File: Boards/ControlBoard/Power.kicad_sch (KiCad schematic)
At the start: 36 parts

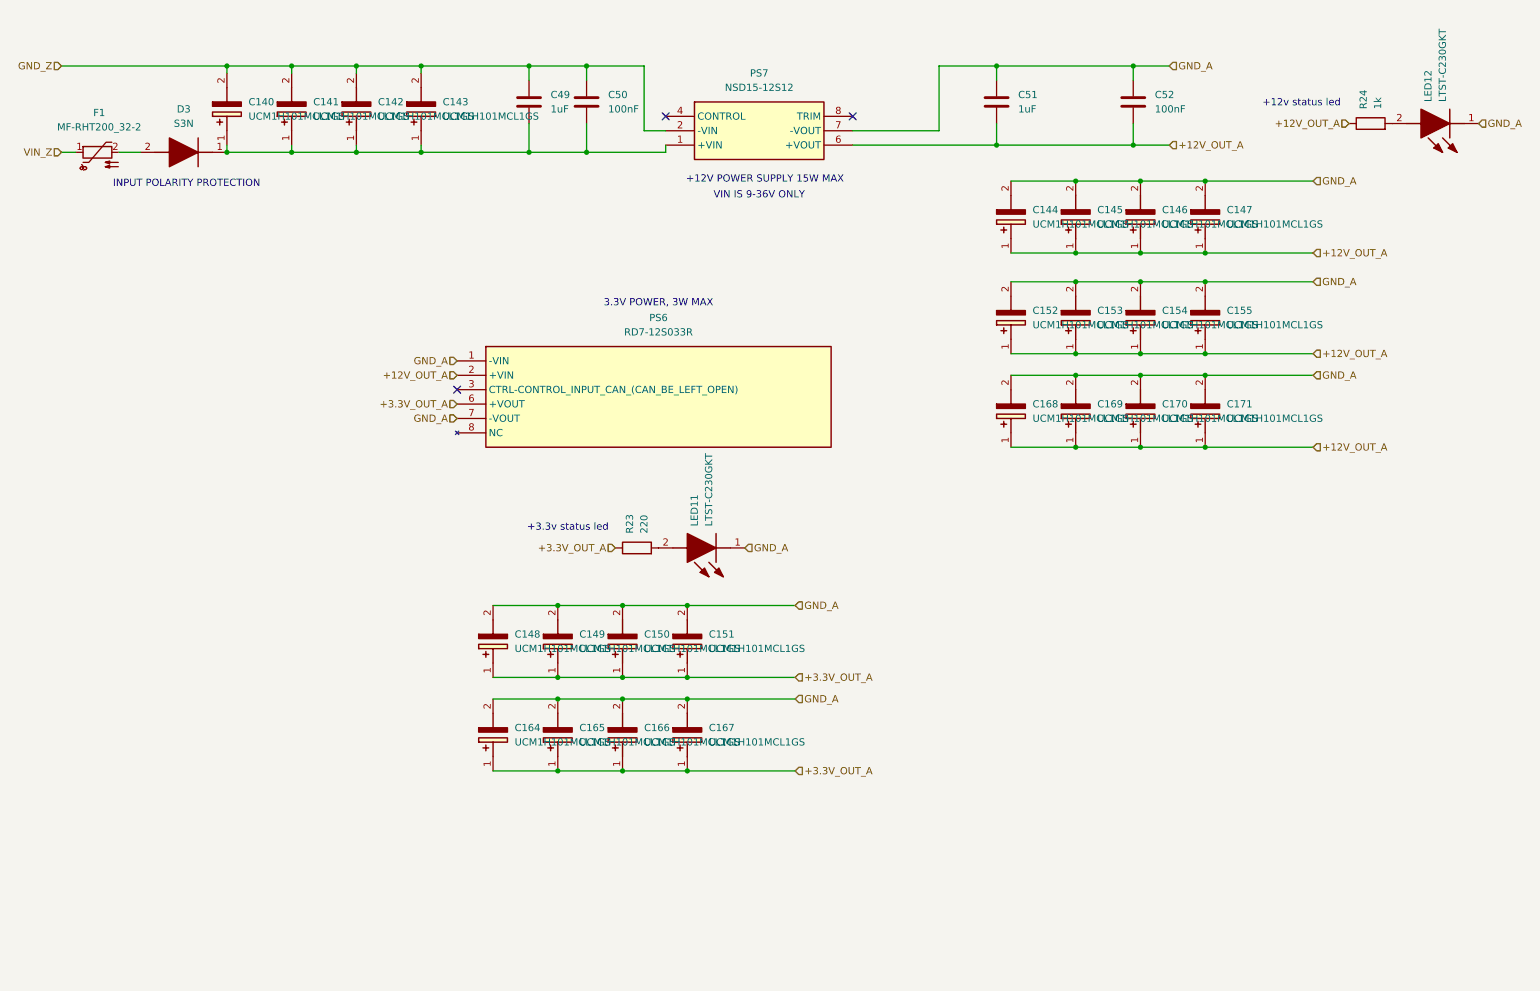
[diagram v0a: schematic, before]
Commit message: layout control boards, add baseplate, refine mechanical layout
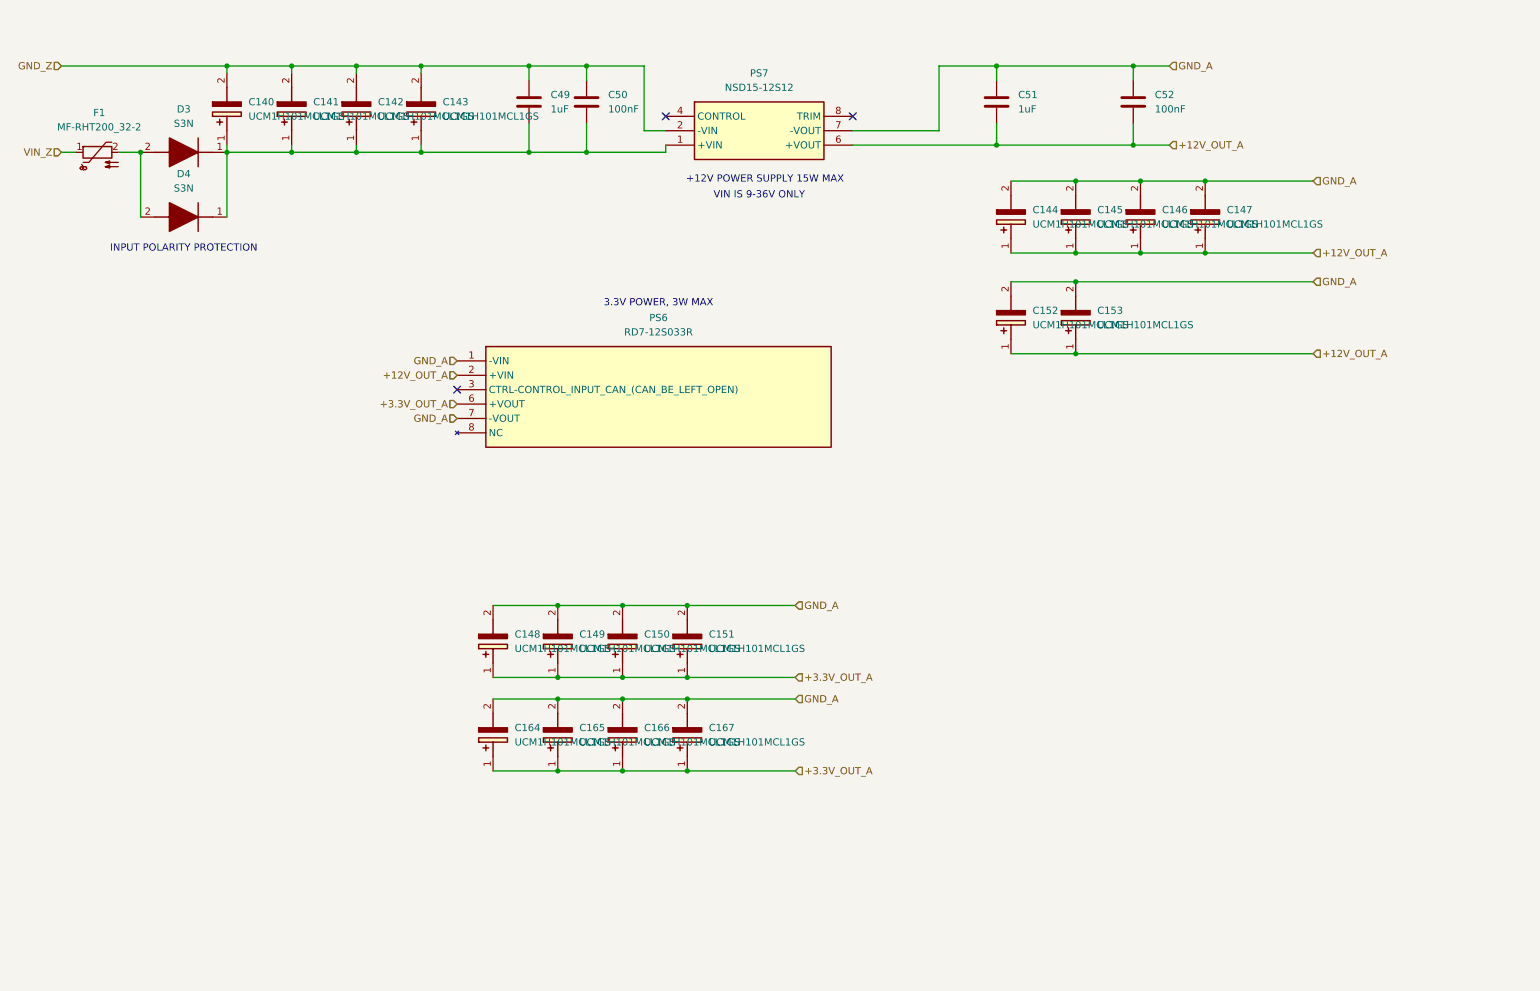
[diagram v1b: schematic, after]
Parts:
- removed C154, C155, C168, C169, C170, C171: UCM1H101MCL1GS, InverterCom:CAPAE660X800N, symbol InverterCom:UCM1H101MCL1GS
- removed LED11, LED12: LTST-C230GKT, InverterCom:LEDC3216X120N, symbol InverterCom:LTST-C230GKT
- removed R23: 220, Resistor_SMD:R_1210_3225Metric_Pad1.30x2.65mm_HandSolder, symbol Device:R
- removed R24: 1k, Resistor_SMD:R_1210_3225Metric_Pad1.30x2.65mm_HandSolder, symbol Device:R
- added D4: S3N, InverterCom:DIOM8059X265N, symbol InverterCom:S3N
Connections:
- net at C140.1 (+), C141.1 (+), C142.1 (+)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: now also D4.1 (K)
- net at D3.2 (A), F1.2: now also D4.2 (A)
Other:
- note removed: "+12v status led"
- note removed: "+3.3v status led"

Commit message: Layout controlboard, update cad
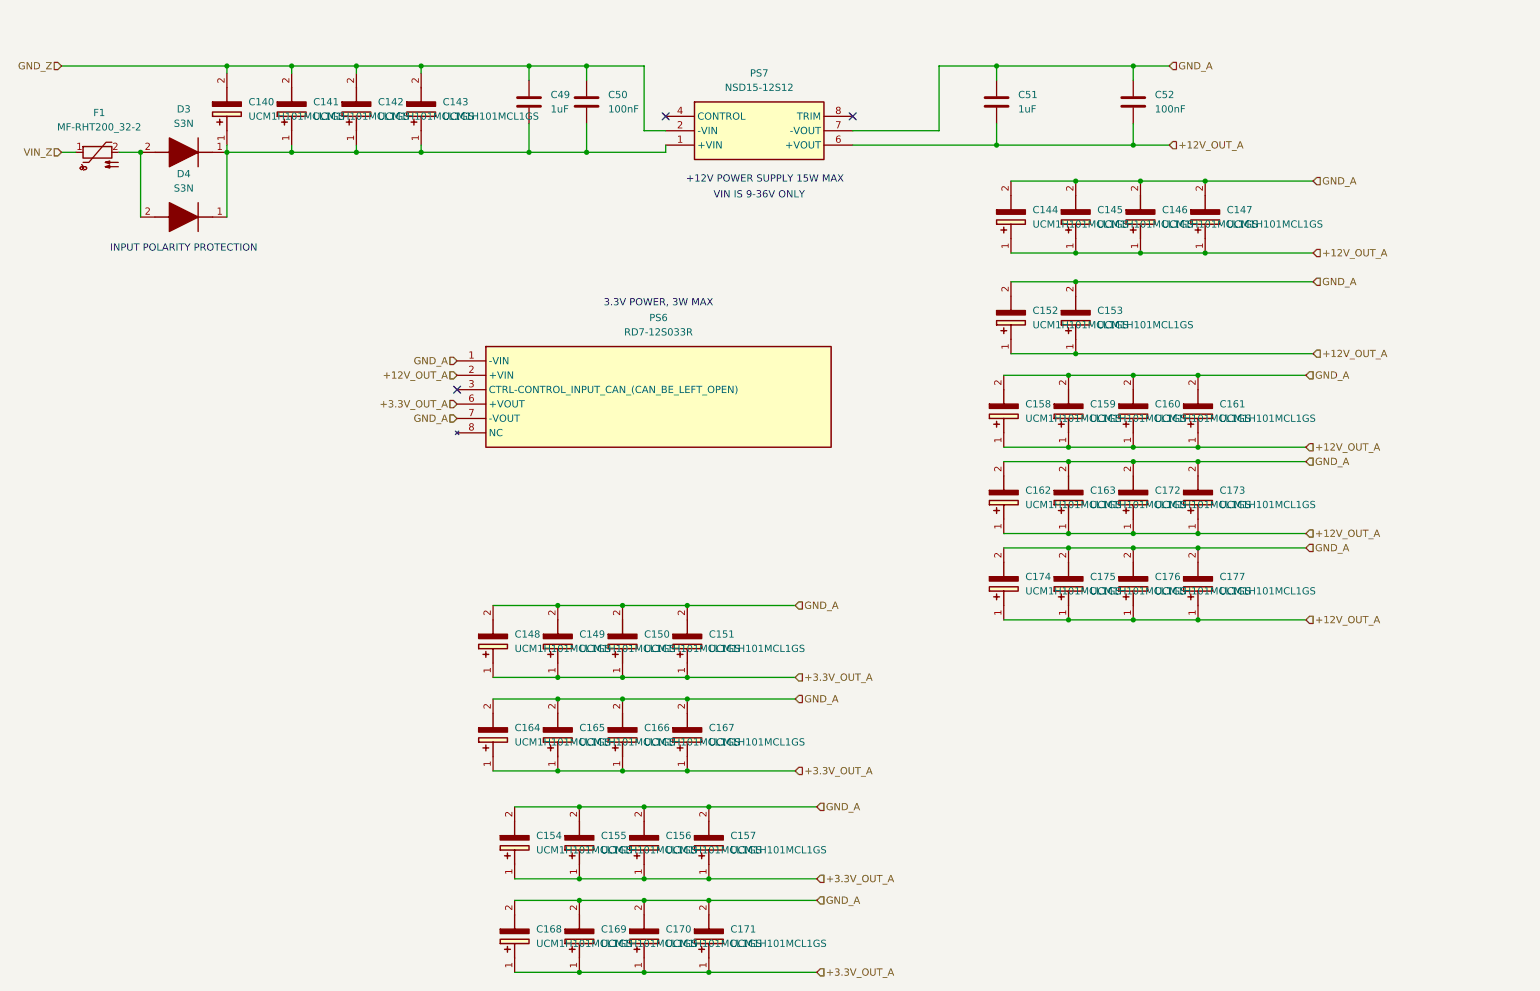
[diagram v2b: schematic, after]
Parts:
- added C154, C155, C156, C157, C158, C159, C160, C161, C162, C163, C168, C169, C170, C171, C172, C173, C174, C175, C176, C177: UCM1H101MCL1GS, InverterCom:CAPAE660X800N, symbol InverterCom:UCM1H101MCL1GS
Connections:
- net +12V_OUT_A: now also C158.1 (+), C159.1 (+), C160.1 (+), C161.1 (+), C162.1 (+), C163.1 (+), C172.1 (+), C173.1 (+), C174.1 (+), C175.1 (+), C176.1 (+), C177.1 (+)
- net +3.3V_OUT_A: now also C154.1 (+), C155.1 (+), C156.1 (+), C157.1 (+), C168.1 (+), C169.1 (+), C170.1 (+), C171.1 (+)
- net GND_A: now also C154.2 (-), C155.2 (-), C156.2 (-), C157.2 (-), C158.2 (-), C159.2 (-), C160.2 (-), C161.2 (-), C162.2 (-), C163.2 (-), C168.2 (-), C169.2 (-), C170.2 (-), C171.2 (-), C172.2 (-), C173.2 (-), C174.2 (-), C175.2 (-), C176.2 (-), C177.2 (-)
